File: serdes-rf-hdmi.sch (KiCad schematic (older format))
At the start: 12 parts, among them J1 HDMI_A, J2 SMA, J3 SMA

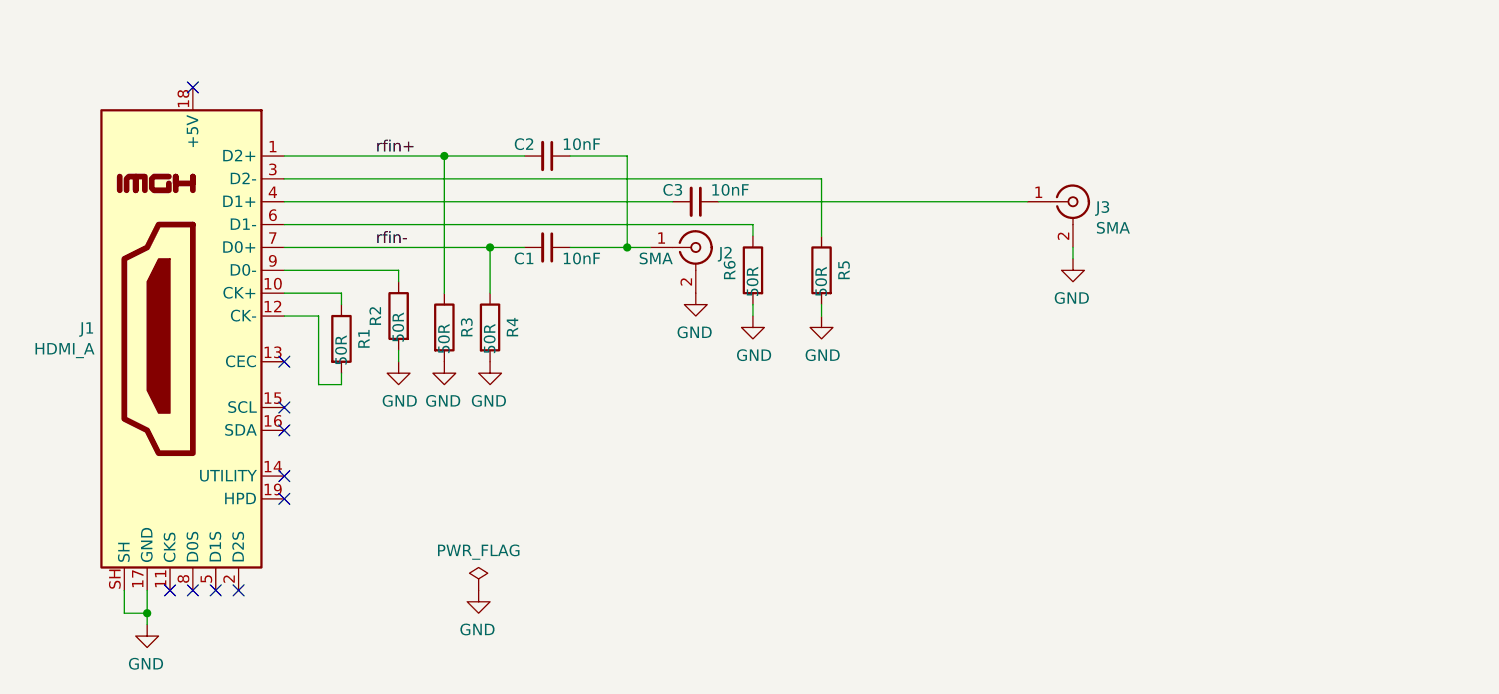
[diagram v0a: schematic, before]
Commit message: Start of rev B design.
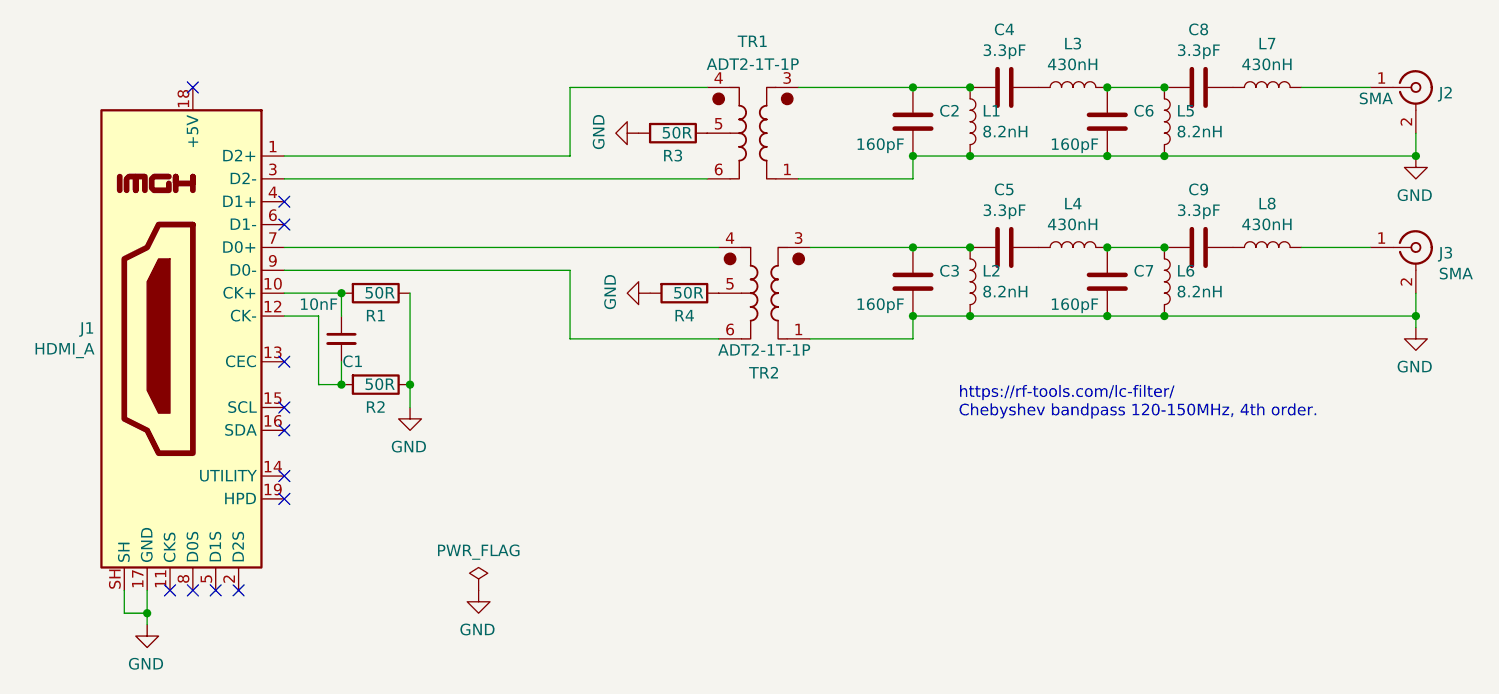
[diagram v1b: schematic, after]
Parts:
- removed C2, C3: 10nF, Capacitor_SMD:C_0402_1005Metric, symbol Device:C_Small
- removed R5, R6: 50R, Resistor_SMD:R_0805_2012Metric, symbol Device:R
- added C2, C3, C6, C7: 160pF, Capacitor_SMD:C_0603_1608Metric_Pad1.08x0.95mm_HandSolder, symbol Device:C
- added C4, C5, C8, C9: 3.3pF, Capacitor_SMD:C_0603_1608Metric_Pad1.08x0.95mm_HandSolder, symbol Device:C
- added L1, L2, L5, L6: 8.2nH, Inductor_SMD:L_0603_1608Metric_Pad1.05x0.95mm_HandSolder, symbol Device:L
- added L3, L4, L7, L8: 430nH, Inductor_SMD:L_0603_1608Metric_Pad1.05x0.95mm_HandSolder, symbol Device:L
- added TR1, TR2: ADT2-1T-1P, serdes-rf-hdmi:XFMR_TC1-1-13M+, symbol Transformer:ADT2-1T-1P
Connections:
- net GND: now also R1.1, R2.1, C2.2, C3.2, C6.2, C7.2, L1.2, L2.2, L5.2, L6.2, TR1.1, TR2.1; no longer R2.2
- net at J2.1 (In): now also L7.2; no longer C1.1
- net at J1.9 (D0-): now also TR2.6; no longer R2.1
- net at J1.10 (CK+): now also C1.1, R1.2; no longer R1.1
- net at J1.12 (CK-): now also C1.2, R2.2; no longer R1.2
- net at J1.3 (D2-): now also TR1.6
- net at J3.1 (In): now also L8.2
- net rfin+: no longer names the net of J1.1 (D2+)
- net rfin+: now also TR1.4; no longer R3.1
- removed net rfin-: C1.2, J1.7 (D0+), R4.1
- new net: J1.7 (D0+), TR2.4
- new net: C3.1, C5.2, L2.1, TR2.3
- new net: R4.1, TR2.5
- new net: C2.1, C4.2, L1.1, TR1.3
- new net: R3.1, TR1.5
- new net: C6.1, C8.2, L3.2, L5.1
- new net: C4.1, L3.1
- new net: C8.1, L7.1
- new net: C7.1, C9.2, L4.2, L6.1
- new net: C5.1, L4.1
- new net: C9.1, L8.1
- no-connect marks 10 -> 12
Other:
- note added: "https://rf-tools.com/lc-filter/\nChebyshev bandpass 120-150MHz, 4th order."
- moved on the sheet: J2, J3, R1

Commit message: Rev B complete
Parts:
- removed TR1, TR2: ADT2-1T-1P, serdes-rf-hdmi:XFMR_TC1-1-13M+, symbol Transformer:ADT2-1T-1P
- added TR1, TR2: TC1-1TX+, serdes-rf-hdmi:XFMR_TC1-1-13M+, symbol TC1-1TX_:TC1-1TX+
- C1: footprint Capacitor_SMD:C_0402_1005Metric -> Capacitor_SMD:C_0603_1608Metric
- renumbered J3 to J2, J2 to J3
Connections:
- net GND: now also TR1.6, TR2.6
- net rfa+: now reaches J1.1 (D2+)
- net rfa+: now also TR1.3
- net rfa-: now reaches J1.3 (D2-)
- net rfa-: now also TR1.1
- net rfb+: now reaches J1.7 (D0+)
- net rfb+: now also TR2.3
- net rfb-: now reaches J1.9 (D0-)
- net rfb-: now also TR2.1
- net at C3.1, C5.2, L2.1: now also TR2.4
- net at R4.1: now also TR2.2
- net at C2.1, C4.2, L1.1: now also TR1.4
- net at R3.1: now also TR1.2
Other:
- moved on the sheet: R3, R4
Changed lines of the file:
@@
 Sheet 1 1
 Title "HDMI RF Test Board"
-Date "2021-08-29"
-Rev "A"
+Date "2021-10-07"
+Rev "B"
 Comp "Mobilinkd LLC"
 Comment1 ""
@@
 $EndDescr
 $Comp
-L Connector:Conn_Coaxial J2
+L Connector:Conn_Coaxial J3
 U 1 1 61266A15
 P 8050 1150
-F 0 "J2" H 8150 1125 50  0000 L CNN
+F 0 "J3" H 8150 1125 50  0000 L CNN
 F 1 "SMA" H 7800 1100 50  0000 L CNN
 F 2 "Connector_Coaxial:SMA_Samtec_SMA-J-P-X-ST-EM1_EdgeMount" H 8050 1150 50  0001 C CNN
@@
 $EndComp
 $Comp
-L Connector:Conn_Coaxial J3
+L Connector:Conn_Coaxial J2
 U 1 1 61274BE5
 P 8050 1850
-F 0 "J3" H 8150 1825 50  0000 L CNN
+F 0 "J2" H 8150 1825 50  0000 L CNN
 F 1 "SMA" H 8150 1734 50  0000 L CNN
 F 2 "Connector_Coaxial:SMA_Samtec_SMA-J-P-X-ST-EM1_EdgeMount" H 8050 1850 50  0001 C CNN
@@
 F 0 "C1" H 3400 2150 50  0000 C CNN
 F 1 "10nF" H 3250 2400 50  0000 C CNN
-F 2 "Capacitor_SMD:C_0402_1005Metric" H 3350 2250 50  0001 C CNN
+F 2 "Capacitor_SMD:C_0603_1608Metric" H 3350 2250 50  0001 C CNN
 F 3 "~" H 3350 2250 50  0001 C CNN
 	1    3350 2250
@@
 	3650 2550 3650 2450
 Connection ~ 3650 2450
-$Comp
-L Transformer:ADT2-1T-1P TR2
-U 1 1 615E1C9B
-P 5200 2050
-F 0 "TR2" H 5200 1700 50  0000 C CNN
-F 1 "ADT2-1T-1P" H 5200 1800 50  0000 C CNN
-F 2 "serdes-rf-hdmi:XFMR_TC1-1-13M+" H 5200 1700 50  0001 C CNN
-F 3 "https://www.minicircuits.com/pdfs/ADT2-1T-1P+.pdf" H 5200 2050 50  0001 C CNN
-	1    5200 2050
-	-1   0    0    -1
-$EndComp
-$Comp
-L Transformer:ADT2-1T-1P TR1
-U 1 1 615EC9E6
-P 5150 1350
-F 0 "TR1" H 5150 1750 50  0000 C CNN
-F 1 "ADT2-1T-1P" H 5150 1650 50  0000 C CNN
-F 2 "serdes-rf-hdmi:XFMR_TC1-1-13M+" H 5150 1000 50  0001 C CNN
-F 3 "https://www.minicircuits.com/pdfs/ADT2-1T-1P+.pdf" H 5150 1350 50  0001 C CNN
-	1    5150 1350
-	-1   0    0    -1
-$EndComp
 Connection ~ 3350 2050
 Connection ~ 3350 2450
@@
 L Device:R R4
 U 1 1 615F5C9B
-P 4850 2050
-F 0 "R4" V 4950 2050 50  0000 C CNN
-F 1 "50R" V 4850 2000 50  0000 L CNN
-F 2 "Resistor_SMD:R_0805_2012Metric" V 4780 2050 50  0001 C CNN
-F 3 "~" H 4850 2050 50  0001 C CNN
-	1    4850 2050
+P 4800 2050
+F 0 "R4" V 4900 2050 50  0000 C CNN
+F 1 "50R" V 4800 2000 50  0000 L CNN
+F 2 "Resistor_SMD:R_0805_2012Metric" V 4730 2050 50  0001 C CNN
+F 3 "~" H 4800 2050 50  0001 C CNN
+	1    4800 2050
 	0    1    1    0
 $EndComp
@@
 L power:GND #PWR05
 U 1 1 615F6835
-P 4700 2050
-F 0 "#PWR05" H 4700 1800 50  0001 C CNN
-F 1 "GND" H 4705 1877 50  0000 C CNN
-F 2 "" H 4700 2050 50  0001 C CNN
-F 3 "" H 4700 2050 50  0001 C CNN
-	1    4700 2050
+P 4650 2050
+F 0 "#PWR05" H 4650 1800 50  0001 C CNN
+F 1 "GND" H 4655 1877 50  0000 C CNN
+F 2 "" H 4650 2050 50  0001 C CNN
+F 3 "" H 4650 2050 50  0001 C CNN
+	1    4650 2050
 	0    1    -1   0
 $EndComp
@@
 L Device:R R3
 U 1 1 615F9D2D
-P 4800 1350
-F 0 "R3" V 4900 1350 50  0000 C CNN
-F 1 "50R" V 4800 1300 50  0000 L CNN
-F 2 "Resistor_SMD:R_0805_2012Metric" V 4730 1350 50  0001 C CNN
-F 3 "~" H 4800 1350 50  0001 C CNN
-	1    4800 1350
+P 4750 1350
+F 0 "R3" V 4850 1350 50  0000 C CNN
+F 1 "50R" V 4750 1300 50  0000 L CNN
+F 2 "Resistor_SMD:R_0805_2012Metric" V 4680 1350 50  0001 C CNN
+F 3 "~" H 4750 1350 50  0001 C CNN
+	1    4750 1350
 	0    1    1    0
 $EndComp
@@
 L power:GND #PWR04
 U 1 1 615F9D33
-P 4650 1350
-F 0 "#PWR04" H 4650 1100 50  0001 C CNN
-F 1 "GND" H 4655 1177 50  0000 C CNN
-F 2 "" H 4650 1350 50  0001 C CNN
-F 3 "" H 4650 1350 50  0001 C CNN
-	1    4650 1350
+P 4600 1350
+F 0 "#PWR04" H 4600 1100 50  0001 C CNN
+F 1 "GND" H 4605 1177 50  0000 C CNN
+F 2 "" H 4600 1350 50  0001 C CNN
+F 3 "" H 4600 1350 50  0001 C CNN
+	1    4600 1350
 	0    1    -1   0
 $EndComp
@@
 Text Notes 6050 2600 0    50   ~ 0
 https://rf-tools.com/lc-filter/\nChebyshev bandpass 120-150MHz, 4th order.
+Wire Wire Line
+	4900 1350 4950 1350
+Wire Wire Line
+	4950 2050 5000 2050
+$Comp
+L TC1-1TX_:TC1-1TX+ TR1
+U 1 1 61672048
+P 5150 1350
+F 0 "TR1" H 5150 1017 50  0000 C CNN
+F 1 "TC1-1TX+" H 5150 1000 50  0001 C CNN
+F 2 "serdes-rf-hdmi:XFMR_TC1-1-13M+" H 5050 1700 50  0001 C CNN
+F 3 "https://www.mouser.com/datasheet/2/1030/TC1_1TX_2b-1701474.pdf" H 5150 1350 50  0001 C CNN
+	1    5150 1350
+	-1   0    0    1
+$EndComp
+$Comp
+L TC1-1TX_:TC1-1TX+ TR2
+U 1 1 61674845
+P 5200 2050
+F 0 "TR2" H 5200 2339 50  0000 C CNN
+F 1 "TC1-1TX+" H 5200 1700 50  0001 C CNN
+F 2 "serdes-rf-hdmi:XFMR_TC1-1-13M+" H 5100 2400 50  0001 C CNN
+F 3 "https://www.mouser.com/datasheet/2/1030/TC1_1TX_2b-1701474.pdf" H 5200 2050 50  0001 C CNN
+	1    5200 2050
+	-1   0    0    1
+$EndComp
+Text Label 3750 1850 0    50   ~ 0
+rfb+
+Text Label 3750 1950 0    50   ~ 0
+rfb-
+Text Label 3700 1550 0    50   ~ 0
+rfa-
+Text Label 3700 1450 0    50   ~ 0
+rfa+
 $EndSCHEMATC

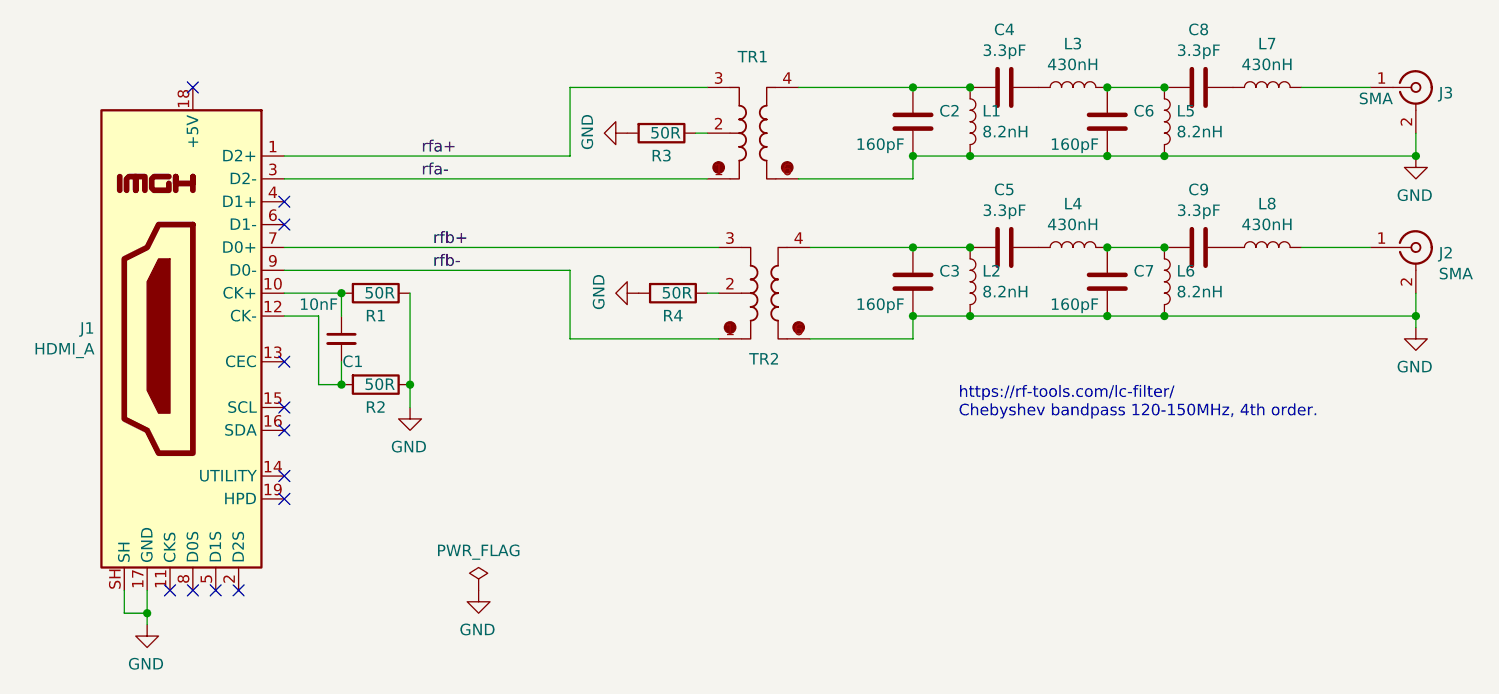
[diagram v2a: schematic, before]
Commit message: Fix bandpass filter and add coupling caps.  Update image and README.
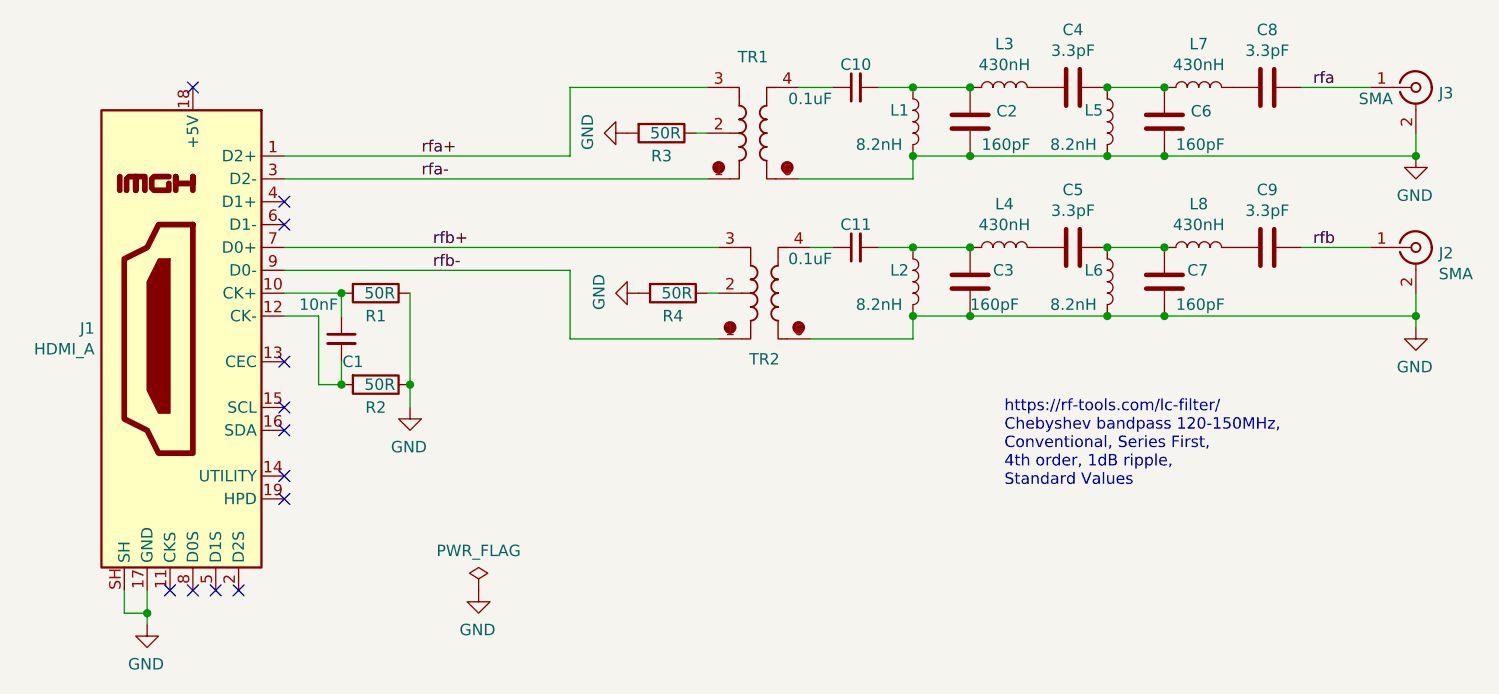
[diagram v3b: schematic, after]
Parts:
- added C10, C11: 0.1uF, Capacitor_SMD:C_0603_1608Metric, symbol Device:C_Small
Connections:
- net at L7.2: now also C8.2; no longer J3.1 (In)
- net at L8.2: now also C9.2; no longer J2.1 (In)
- net at C2.1, L1.1: now also L3.1, C10.2; no longer C4.2, TR1.4
- net at C6.1, L5.1: now also C4.1, L7.1; no longer C8.2, L3.2
- net rfa: now reaches C8.1
- net rfa: now also J3.1 (In); no longer L7.1
- net at C3.1, L2.1: now also L4.1, C11.2; no longer C5.2, TR2.4
- net at C7.1, L6.1: now also C5.1, L8.1; no longer C9.2, L4.2
- net rfb: now reaches C9.1
- net rfb: now also J2.1 (In); no longer L8.1
- new net: C4.2, L3.2
- new net: C5.2, L4.2
- new net: C10.1, TR1.4
- new net: C11.1, TR2.4
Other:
- note added: "https://rf-tools.com/lc-filter/\nChebyshev bandpass 120-150MHz,\nConventional, Series First,\n4th order, 1dB ripple,\nStandard Values\n"
- note removed: "https://rf-tools.com/lc-filter/\nChebyshev bandpass 120-150MHz, 4th order."
- moved on the sheet: C2, C3, C4, C5, C6, C7, C8, C9, L1, L2, L3, L4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
